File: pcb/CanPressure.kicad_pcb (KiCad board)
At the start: 2 copper layers, 66.4 x 28.1 mm, 18 parts, among them IC101 ATTINY3224-SS, P102 CONN_5, P103 CAN, U101 MCP2515, U102 TJA1050, U103 NCP1117ST50T3G, U105 BMP280, X101 8MHz

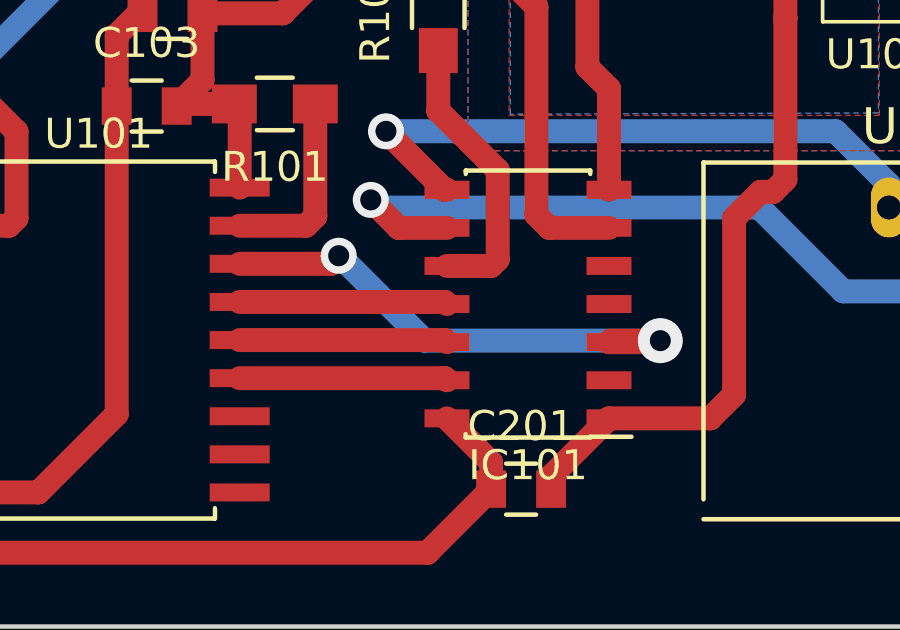
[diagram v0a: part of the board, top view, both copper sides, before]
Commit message: Working in test harness  with a MCP2515 module
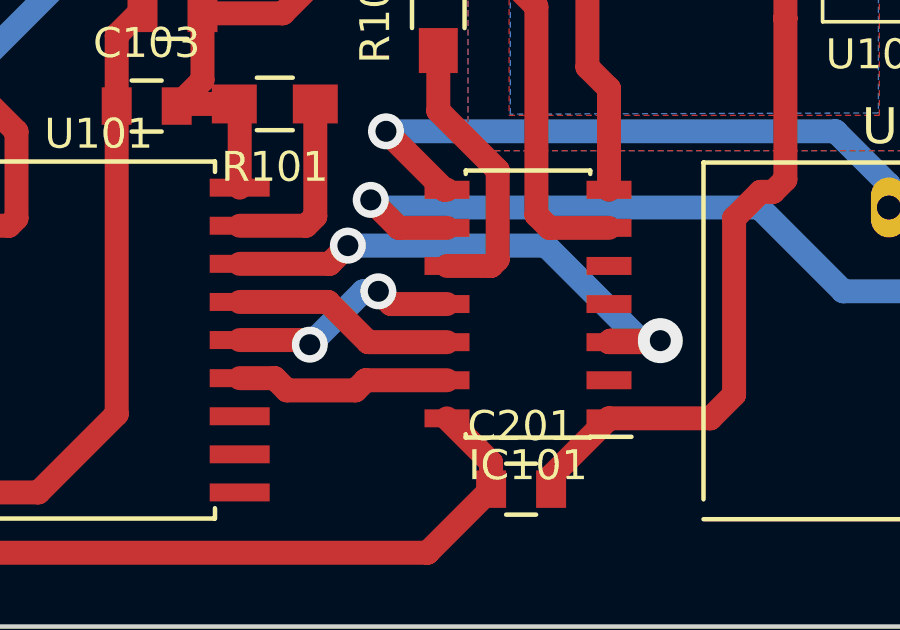
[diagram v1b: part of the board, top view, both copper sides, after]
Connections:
- IC101 pad 11: MISO -> MOSI
- IC101 pad 12: MOSI -> MISO
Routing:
- net MOSI: track 6.94 -> 7.89 mm, vias 0 -> 2
- net MISO: track 6.94 -> 7.47 mm
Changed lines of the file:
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@@
     (thickness 1.6)
     (drawings 10)
-    (tracks 189)
+    (tracks 199)
     (zones 0)
     (modules 18)
@@
       (net 18 UDPI))
     (pad 11 smd rect (at 2.7 0 180) (size 1.5 0.6) (layers F.Cu F.Paste F.Mask)
+      (net 5 MOSI))
+    (pad 12 smd rect (at 2.7 -1.27 180) (size 1.5 0.6) (layers F.Cu F.Paste F.Mask)
       (net 2 MISO))
-    (pad 12 smd rect (at 2.7 -1.27 180) (size 1.5 0.6) (layers F.Cu F.Paste F.Mask)
-      (net 5 MOSI))
     (pad 13 smd rect (at 2.7 -2.54 180) (size 1.5 0.6) (layers F.Cu F.Paste F.Mask)
       (net 1 SCK))
@@
   (gr_line (start 171.066 119.498) (end 173.606 119.498) (angle 90) (layer Dwgs.User) (width 0.2))
   (gr_line (start 98.044 272.542) (end 98.044 272.796) (angle 90) (layer Dwgs.User) (width 0.2))
-  (segment (start 139.65 128.624) (end 146.49 128.624) (width 0.8) (layer F.Cu) (net 1) (status 30))
-  (segment (start 146.49 128.624) (end 146.56 128.694) (width 0.8) (layer F.Cu) (net 1) (status 30))
-  (segment (start 139.65 126.084) (end 146.49 126.084) (width 0.8) (layer F.Cu) (net 2) (status 30))
-  (segment (start 146.49 126.084) (end 146.56 126.154) (width 0.8) (layer F.Cu) (net 2) (status 30))
+  (segment (start 146.56 128.694) (end 143.848 128.694) (width 0.8) (layer F.Cu) (net 1) (status 400000))
+  (segment (start 140.816 128.624) (end 139.65 128.624) (width 0.8) (layer F.Cu) (net 1) (status 800000))
+  (segment (start 141.224 129.032) (end 140.816 128.624) (width 0.8) (layer F.Cu) (net 1))
+  (segment (start 143.51 129.032) (end 141.224 129.032) (width 0.8) (layer F.Cu) (net 1))
+  (segment (start 143.848 128.694) (end 143.51 129.032) (width 0.8) (layer F.Cu) (net 1))
+  (segment (start 139.65 126.084) (end 142.594 126.084) (width 0.8) (layer F.Cu) (net 2) (status 400000))
+  (segment (start 143.934 127.424) (end 146.56 127.424) (width 0.8) (layer F.Cu) (net 2) (status 800000))
+  (segment (start 142.594 126.084) (end 143.934 127.424) (width 0.8) (layer F.Cu) (net 2))
+  (segment (start 139.65 124.814) (end 142.648 124.814) (width 0.8) (layer F.Cu) (net 3) (status 400000))
+  (segment (start 153.028 127.374) (end 153.67 127.374) (width 0.8) (layer B.Cu) (net 3))
+  (segment (start 149.86 124.206) (end 153.028 127.374) (width 0.8) (layer B.Cu) (net 3))
+  (segment (start 143.256 124.206) (end 149.86 124.206) (width 0.8) (layer B.Cu) (net 3))
+  (via (at 143.256 124.206) (size 1.2) (drill 0.7) (layers F.Cu B.Cu) (net 3))
+  (segment (start 142.648 124.814) (end 143.256 124.206) (width 0.8) (layer F.Cu) (net 3))
   (segment (start 153.67 127.374) (end 152.01 127.374) (width 0.8) (layer F.Cu) (net 3) (status 20))
   (segment (start 152.01 127.374) (end 151.96 127.424) (width 0.8) (layer F.Cu) (net 3) (status 30))
-  (segment (start 142.95 124.544) (end 142.98 124.544) (width 0.8) (layer B.Cu) (net 3))
-  (segment (start 142.68 124.814) (end 142.95 124.544) (width 0.8) (layer F.Cu) (net 3))
-  (via (at 142.95 124.544) (size 1.2) (drill 0.7) (layers F.Cu B.Cu) (net 3))
-  (segment (start 139.65 124.814) (end 142.68 124.814) (width 0.8) (layer F.Cu) (net 3) (status 10))
   (segment (start 153.62 127.424) (end 151.96 127.424) (width 0.8) (layer F.Cu) (net 3) (status 20))
   (segment (start 153.67 127.374) (end 153.62 127.424) (width 0.8) (layer F.Cu) (net 3))
   (via (at 153.67 127.374) (size 1.5) (drill 0.7) (layers F.Cu B.Cu) (net 3))
-  (segment (start 145.81 127.374) (end 153.67 127.374) (width 0.8) (layer B.Cu) (net 3))
-  (segment (start 142.98 124.544) (end 145.81 127.374) (width 0.8) (layer B.Cu) (net 3))
   (segment (start 164.21 118.334) (end 164.816 118.334) (width 0.8) (layer B.Cu) (net 4))
   (segment (start 166.37 119.888) (end 166.37 122.936) (width 0.8) (layer B.Cu) (net 4))
@@
   (segment (start 121.66 132.894) (end 121.66 128.084) (width 0.8) (layer F.Cu) (net 4) (status 30))
   (segment (start 121.66 128.084) (end 121.77 127.974) (width 0.8) (layer F.Cu) (net 4) (status 30))
-  (segment (start 139.65 127.354) (end 146.49 127.354) (width 0.8) (layer F.Cu) (net 5) (status 30))
-  (segment (start 146.49 127.354) (end 146.56 127.424) (width 0.8) (layer F.Cu) (net 5) (status 30))
+  (segment (start 139.65 127.354) (end 141.832 127.354) (width 0.8) (layer F.Cu) (net 5) (status 400000))
+  (segment (start 144.696 126.154) (end 146.56 126.154) (width 0.8) (layer F.Cu) (net 5) (status 800000))
+  (segment (start 144.272 125.73) (end 144.696 126.154) (width 0.8) (layer F.Cu) (net 5))
+  (via (at 144.272 125.73) (size 1.2) (drill 0.7) (layers F.Cu B.Cu) (net 5))
+  (segment (start 143.764 125.73) (end 144.272 125.73) (width 0.8) (layer B.Cu) (net 5))
+  (segment (start 141.986 127.508) (end 143.764 125.73) (width 0.8) (layer B.Cu) (net 5))
+  (via (at 141.986 127.508) (size 1.2) (drill 0.7) (layers F.Cu B.Cu) (net 5))
+  (segment (start 141.832 127.354) (end 141.986 127.508) (width 0.8) (layer F.Cu) (net 5))
   (segment (start 125.5 132.974) (end 123.94 132.974) (width 0.8) (layer F.Cu) (net 6) (status 30))
   (segment (start 123.94 132.974) (end 123.86 132.894) (width 0.8) (layer F.Cu) (net 6) (status 30))
